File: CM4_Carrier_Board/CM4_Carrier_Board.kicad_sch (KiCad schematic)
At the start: 12 parts, among them J1 Barrel_Jack, J2 DF40C-100DP-0.4V_51_, J3 DF40C-100DP-0.4V_51_, U2 LM2596S-5

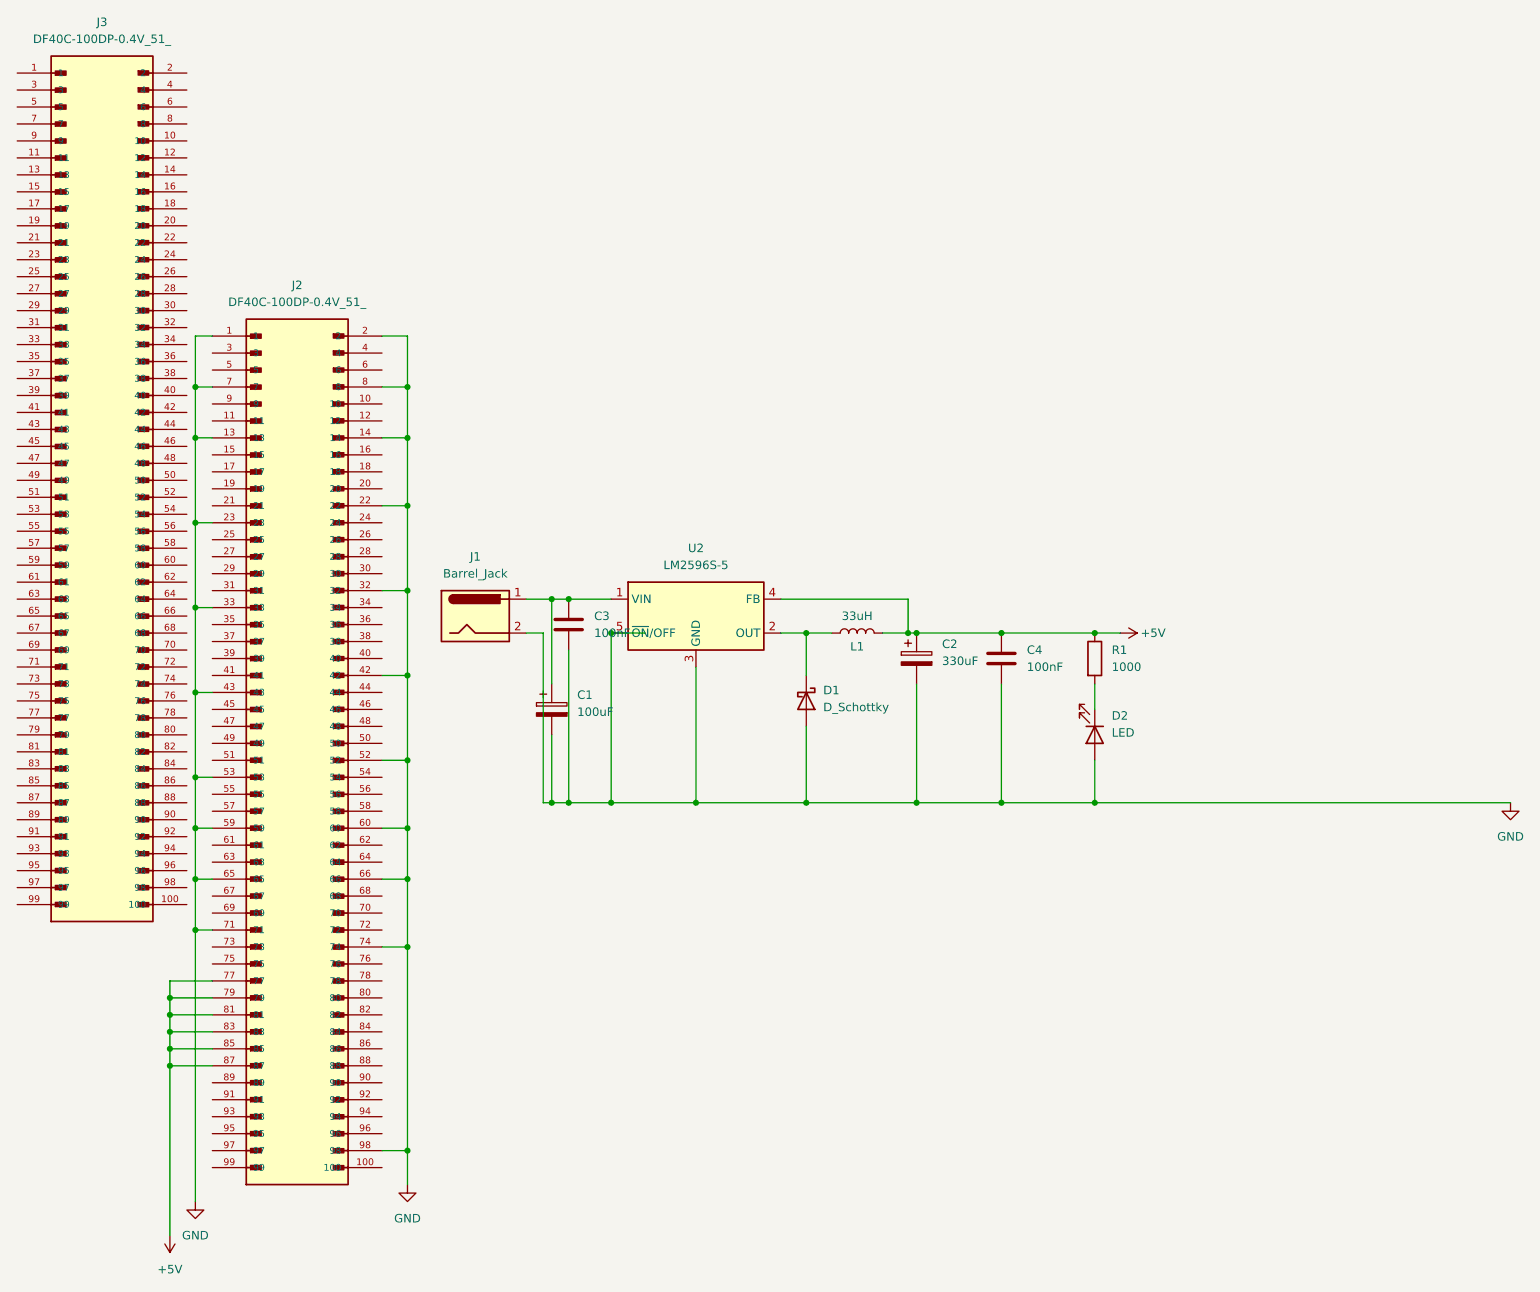
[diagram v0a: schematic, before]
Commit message: Création de la sheet des connecteurs et branchement des signaux de contrôle
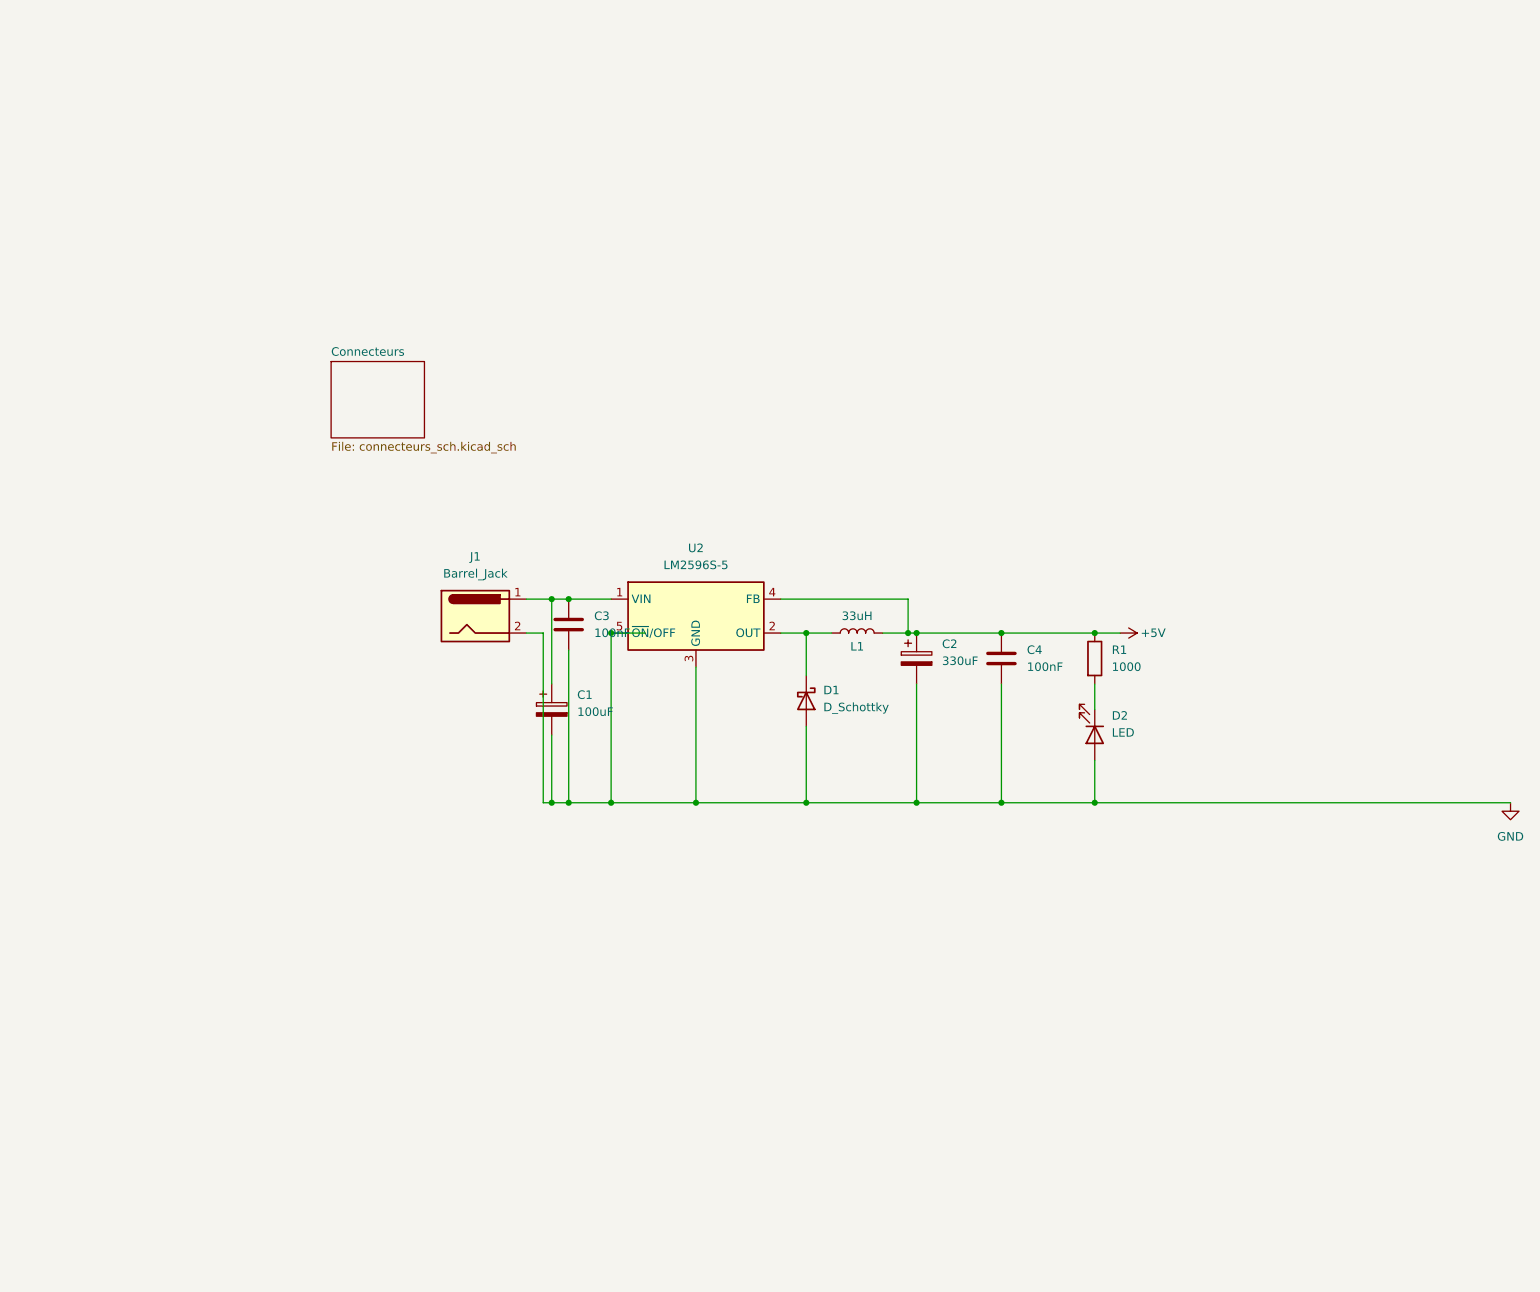
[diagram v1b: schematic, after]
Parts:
- removed J2, J3: DF40C-100DP-0.4V_51_, HIROSE_DF40C-100DP-0.4V_51_, symbol DF40C-100DP-0.4V_51_:DF40C-100DP-0.4V_51_
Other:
- added sheet Connecteurs (connecteurs_sch.kicad_sch)

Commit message: Ajout de la sheet pour le PCIe
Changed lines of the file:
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@@
-	)
-	(junction
-		(at 93.98 99.06)
-		(diameter 0)
-		(color 0 0 0 0)
 	)
 	(junction
@@
 	)
 	(junction
+		(at 123.19 99.06)
+		(diameter 0)
+		(color 0 0 0 0)
+	)
+	(junction
 		(at 152.4 99.06)
 		(diameter 0)
@@
 	)
 	(junction
-		(at 123.19 99.06)
-		(diameter 0)
-		(color 0 0 0 0)
-	)
-	(junction
 		(at 123.19 124.46)
 		(diameter 0)
@@
 	)
 	(junction
+		(at 204.47 124.46)
+		(diameter 0)
+		(color 0 0 0 0)
+	)
+	(junction
 		(at 139.7 124.46)
 		(diameter 0)
@@
 		(color 0 0 0 0)
 	)
-	(wire
-		(pts
-			(xy 166.37 124.46) (xy 228.6 124.46)
+	(junction
+		(at 91.44 93.98)
+		(diameter 0)
+		(color 0 0 0 0)
+	)
+	(wire
+		(pts
+			(xy 166.37 124.46) (xy 204.47 124.46)
 		)
 		(stroke
@@
 	(wire
 		(pts
-			(xy 93.98 99.06) (xy 99.06 99.06)
+			(xy 204.47 124.46) (xy 228.6 124.46)
 		)
 		(stroke
@@
 	(wire
 		(pts
-			(xy 87.63 93.98) (xy 93.98 93.98)
+			(xy 87.63 93.98) (xy 91.44 93.98)
 		)
 		(stroke
@@
 	(wire
 		(pts
+			(xy 93.98 93.98) (xy 91.44 93.98)
+		)
+		(stroke
+			(width 0)
+			(type default)
+		)
+	)
+	(wire
+		(pts
 			(xy 83.82 99.06) (xy 83.82 124.46)
 		)
@@
 	(wire
 		(pts
+			(xy 87.63 124.46) (xy 93.98 124.46)
+		)
+		(stroke
+			(width 0)
+			(type default)
+		)
+	)
+	(wire
+		(pts
 			(xy 119.38 99.06) (xy 123.19 99.06)
 		)
@@
 	(wire
 		(pts
-			(xy 87.63 124.46) (xy 93.98 124.46)
+			(xy 106.68 124.46) (xy 123.19 124.46)
 		)
 		(stroke
@@
 		(pts
 			(xy 87.63 101.6) (xy 87.63 124.46)
-		)
-		(stroke
-			(width 0)
-			(type default)
-		)
-	)
-	(wire
-		(pts
-			(xy 106.68 124.46) (xy 123.19 124.46)
 		)
 		(stroke
@@
 		(in_pos_files yes)
 		(dnp no)
-		(fields_autoplaced yes)
 		(property "Reference" "C3"
-			(at 91.44 96.5199 0)
+			(at 90.424 96.774 0)
 			(show_name no)
 			(do_not_autoplace no)
@@
 		)
 		(property "Value" "100nF"
-			(at 91.44 99.0599 0)
+			(at 87.884 100.838 0)
 			(show_name no)
 			(do_not_autoplace no)
@@
 	)
 	(symbol
+		(lib_id "power:PWR_FLAG")
+		(at 91.44 93.98 0)
+		(unit 1)
+		(body_style 1)
+		(exclude_from_sim no)
+		(in_bom yes)
+		(on_board yes)
+		(in_pos_files yes)
+		(dnp no)
+		(fields_autoplaced yes)
+		(property "Reference" "#FLG01"
+			(at 91.44 92.075 0)
+			(hide yes)
+			(show_name no)
+			(do_not_autoplace no)
+			(effects
+				(font
+					(size 1.27 1.27)
+				)
+			)
+		)
+		(property "Value" "PWR_FLAG"
+			(at 91.44 88.9 0)
+			(show_name no)
+			(do_not_autoplace no)
+			(effects
+				(font
+					(size 1.27 1.27)
+				)
+			)
+		)
+		(property "Footprint" ""
+			(at 91.44 93.98 0)
+			(hide yes)
+			(show_name no)
+			(do_not_autoplace no)
+			(effects
+				(font
+					(size 1.27 1.27)
+				)
+			)
+		)
+		(property "Datasheet" ""
+			(at 91.44 93.98 0)
+			(hide yes)
+			(show_name no)
+			(do_not_autoplace no)
+			(effects
+				(font
+					(size 1.27 1.27)
+				)
+			)
+		)
+		(property "Description" "Special symbol for telling ERC where power comes from"
+			(at 91.44 93.98 0)
+			(hide yes)
+			(show_name no)
+			(do_not_autoplace no)
+			(effects
+				(font
+					(size 1.27 1.27)
+				)
+			)
+		)
+		(pin "1"
+		)
+		(instances
+			(project "CM4_Carrier_Board"
+				(path "/f7b1e63c-7624-492a-bdf8-5574ba799d92"
+					(reference "#FLG01")
+					(unit 1)
+				)
+			)
+		)
+	)
+	(symbol
 		(lib_id "Device:D_Schottky")
 		(at 123.19 109.22 270)
@@
 					(unit 1)
 				)
+			)
+		)
+	)
+	(symbol
+		(lib_id "power:PWR_FLAG")
+		(at 204.47 124.46 0)
+		(unit 1)
+		(body_style 1)
+		(exclude_from_sim no)
+		(in_bom yes)
+		(on_board yes)
+		(in_pos_files yes)
+		(dnp no)
+		(fields_autoplaced yes)
+		(property "Reference" "#FLG02"
+			(at 204.47 122.555 0)
+			(hide yes)
+			(show_name no)
+			(do_not_autoplace no)
+			(effects
+				(font
+					(size 1.27 1.27)
+				)
+			)
+		)
+		(property "Value" "PWR_FLAG"
+			(at 204.47 119.38 0)
+			(show_name no)
+			(do_not_autoplace no)
+			(effects
+				(font
+					(size 1.27 1.27)
+				)
+			)
+		)
+		(property "Footprint" ""
+			(at 204.47 124.46 0)
+			(hide yes)
+			(show_name no)
+			(do_not_autoplace no)
+			(effects
+				(font
+					(size 1.27 1.27)
+				)
+			)
+		)
+		(property "Datasheet" ""
+			(at 204.47 124.46 0)
+			(hide yes)
+			(show_name no)
+			(do_not_autoplace no)
+			(effects
+				(font
+					(size 1.27 1.27)
+				)
+			)
+		)
+		(property "Description" "Special symbol for telling ERC where power comes from"
+			(at 204.47 124.46 0)
+			(hide yes)
+			(show_name no)
+			(do_not_autoplace no)
+			(effects
+				(font
+					(size 1.27 1.27)
+				)
+			)
+		)
+		(pin "1"
+		)
+		(instances
+			(project "CM4_Carrier_Board"
+				(path "/f7b1e63c-7624-492a-bdf8-5574ba799d92"
+					(reference "#FLG02")
+					(unit 1)
+				)

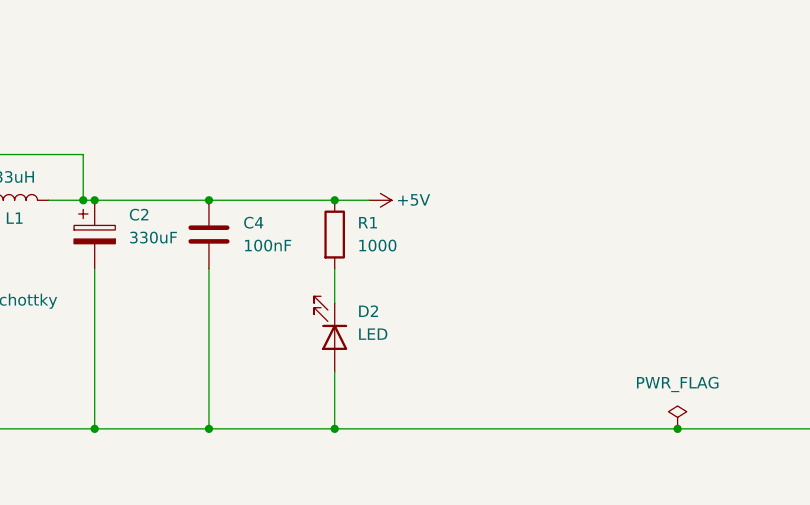
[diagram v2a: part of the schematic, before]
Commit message: Implémentation du cavalier et de la diode d'activation des connecteurs, début d'implémentation du connecteur HDMI
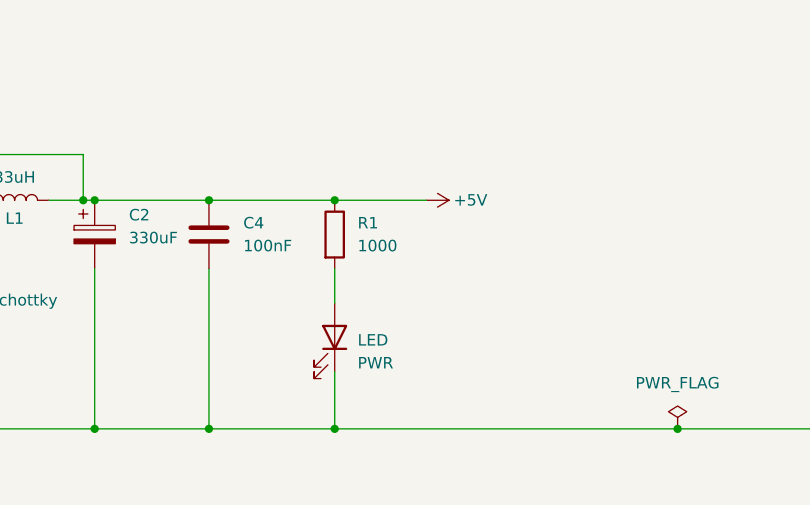
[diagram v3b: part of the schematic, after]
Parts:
- renumbered D2 to PWR
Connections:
- net GND: now also PWR.1 (K); no longer PWR.2 (A)
- net at R1.2: now also PWR.2 (A); no longer PWR.1 (K)
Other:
- moved on the sheet: PWR
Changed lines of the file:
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@@
+	)
+	(junction
+		(at 85.09 124.46)
+		(diameter 0)
+		(color 0 0 0 0)
 	)
 	(junction
@@
 	)
 	(junction
-		(at 85.09 124.46)
-		(diameter 0)
-		(color 0 0 0 0)
-	)
-	(junction
 		(at 166.37 99.06)
 		(diameter 0)
@@
 	(wire
 		(pts
+			(xy 139.7 106.68) (xy 139.7 124.46)
+		)
+		(stroke
+			(width 0)
+			(type default)
+		)
+	)
+	(wire
+		(pts
+			(xy 106.68 104.14) (xy 106.68 124.46)
+		)
+		(stroke
+			(width 0)
+			(type default)
+		)
+	)
+	(wire
+		(pts
+			(xy 166.37 106.68) (xy 166.37 110.49)
+		)
+		(stroke
+			(width 0)
+			(type default)
+		)
+	)
+	(wire
+		(pts
+			(xy 85.09 114.3) (xy 85.09 124.46)
+		)
+		(stroke
+			(width 0)
+			(type default)
+		)
+	)
+	(wire
+		(pts
+			(xy 204.47 124.46) (xy 228.6 124.46)
+		)
+		(stroke
+			(width 0)
+			(type default)
+		)
+	)
+	(wire
+		(pts
+			(xy 85.09 124.46) (xy 87.63 124.46)
+		)
+		(stroke
+			(width 0)
+			(type default)
+		)
+	)
+	(wire
+		(pts
+			(xy 119.38 93.98) (xy 138.43 93.98)
+		)
+		(stroke
+			(width 0)
+			(type default)
+		)
+	)
+	(wire
+		(pts
+			(xy 123.19 99.06) (xy 127 99.06)
+		)
+		(stroke
+			(width 0)
+			(type default)
+		)
+	)
+	(wire
+		(pts
+			(xy 138.43 99.06) (xy 139.7 99.06)
+		)
+		(stroke
+			(width 0)
+			(type default)
+		)
+	)
+	(wire
+		(pts
+			(xy 87.63 93.98) (xy 91.44 93.98)
+		)
+		(stroke
+			(width 0)
+			(type default)
+		)
+	)
+	(wire
+		(pts
+			(xy 139.7 99.06) (xy 152.4 99.06)
+		)
+		(stroke
+			(width 0)
+			(type default)
+		)
+	)
+	(wire
+		(pts
+			(xy 134.62 99.06) (xy 138.43 99.06)
+		)
+		(stroke
+			(width 0)
+			(type default)
+		)
+	)
+	(wire
+		(pts
+			(xy 93.98 99.06) (xy 93.98 124.46)
+		)
+		(stroke
+			(width 0)
+			(type default)
+		)
+	)
+	(wire
+		(pts
+			(xy 152.4 106.68) (xy 152.4 124.46)
+		)
+		(stroke
+			(width 0)
+			(type default)
+		)
+	)
+	(wire
+		(pts
+			(xy 93.98 124.46) (xy 106.68 124.46)
+		)
+		(stroke
+			(width 0)
+			(type default)
+		)
+	)
+	(wire
+		(pts
+			(xy 138.43 93.98) (xy 138.43 99.06)
+		)
+		(stroke
+			(width 0)
+			(type default)
+		)
+	)
+	(wire
+		(pts
+			(xy 123.19 113.03) (xy 123.19 124.46)
+		)
+		(stroke
+			(width 0)
+			(type default)
+		)
+	)
+	(wire
+		(pts
+			(xy 81.28 93.98) (xy 85.09 93.98)
+		)
+		(stroke
+			(width 0)
+			(type default)
+		)
+	)
+	(wire
+		(pts
 			(xy 166.37 124.46) (xy 204.47 124.46)
 		)
@@
 	(wire
 		(pts
-			(xy 139.7 106.68) (xy 139.7 124.46)
-		)
-		(stroke
-			(width 0)
-			(type default)
-		)
-	)
-	(wire
-		(pts
-			(xy 106.68 104.14) (xy 106.68 124.46)
-		)
-		(stroke
-			(width 0)
-			(type default)
-		)
-	)
-	(wire
-		(pts
-			(xy 85.09 114.3) (xy 85.09 124.46)
-		)
-		(stroke
-			(width 0)
-			(type default)
-		)
-	)
-	(wire
-		(pts
-			(xy 204.47 124.46) (xy 228.6 124.46)
-		)
-		(stroke
-			(width 0)
-			(type default)
-		)
-	)
-	(wire
-		(pts
-			(xy 85.09 124.46) (xy 87.63 124.46)
-		)
-		(stroke
-			(width 0)
-			(type default)
-		)
-	)
-	(wire
-		(pts
-			(xy 119.38 93.98) (xy 138.43 93.98)
-		)
-		(stroke
-			(width 0)
-			(type default)
-		)
-	)
-	(wire
-		(pts
-			(xy 123.19 99.06) (xy 127 99.06)
-		)
-		(stroke
-			(width 0)
-			(type default)
-		)
-	)
-	(wire
-		(pts
-			(xy 138.43 99.06) (xy 139.7 99.06)
-		)
-		(stroke
-			(width 0)
-			(type default)
-		)
-	)
-	(wire
-		(pts
-			(xy 87.63 93.98) (xy 91.44 93.98)
-		)
-		(stroke
-			(width 0)
-			(type default)
-		)
-	)
-	(wire
-		(pts
-			(xy 139.7 99.06) (xy 152.4 99.06)
-		)
-		(stroke
-			(width 0)
-			(type default)
-		)
-	)
-	(wire
-		(pts
-			(xy 134.62 99.06) (xy 138.43 99.06)
+			(xy 85.09 93.98) (xy 87.63 93.98)
 		)
 		(stroke
@@
 	(wire
 		(pts
-			(xy 166.37 106.68) (xy 166.37 110.49)
-		)
-		(stroke
-			(width 0)
-			(type default)
-		)
-	)
-	(wire
-		(pts
-			(xy 93.98 99.06) (xy 93.98 124.46)
-		)
-		(stroke
-			(width 0)
-			(type default)
-		)
-	)
-	(wire
-		(pts
-			(xy 152.4 106.68) (xy 152.4 124.46)
-		)
-		(stroke
-			(width 0)
-			(type default)
-		)
-	)
-	(wire
-		(pts
-			(xy 93.98 124.46) (xy 106.68 124.46)
-		)
-		(stroke
-			(width 0)
-			(type default)
-		)
-	)
-	(wire
-		(pts
-			(xy 138.43 93.98) (xy 138.43 99.06)
-		)
-		(stroke
-			(width 0)
-			(type default)
-		)
-	)
-	(wire
-		(pts
-			(xy 123.19 113.03) (xy 123.19 124.46)
-		)
-		(stroke
-			(width 0)
-			(type default)
-		)
-	)
-	(wire
-		(pts
-			(xy 81.28 93.98) (xy 85.09 93.98)
-		)
-		(stroke
-			(width 0)
-			(type default)
-		)
-	)
-	(wire
-		(pts
-			(xy 85.09 93.98) (xy 87.63 93.98)
-		)
-		(stroke
-			(width 0)
-			(type default)
-		)
-	)
-	(wire
-		(pts
 			(xy 152.4 124.46) (xy 166.37 124.46)
 		)
@@
 	(wire
 		(pts
-			(xy 166.37 99.06) (xy 170.18 99.06)
+			(xy 166.37 99.06) (xy 176.53 99.06)
 		)
 		(stroke
@@
 	(symbol
 		(lib_id "power:+5V")
-		(at 170.18 99.06 270)
+		(at 176.53 99.06 270)
 		(unit 1)
 		(body_style 1)
@@
 		(dnp no)
 		(property "Reference" "#PWR04"
-			(at 166.37 99.06 0)
+			(at 172.72 99.06 0)
 			(hide yes)
 			(show_name no)
@@
 		)
 		(property "Value" "+5V"
-			(at 173.228 99.06 90)
+			(at 179.578 99.06 90)
 			(show_name no)
 			(do_not_autoplace no)
@@
 		)
 		(property "Footprint" ""
-			(at 170.18 99.06 0)
+			(at 176.53 99.06 0)
 			(hide yes)
 			(show_name no)
@@
 		)
 		(property "Datasheet" ""
-			(at 170.18 99.06 0)
+			(at 176.53 99.06 0)
 			(hide yes)
 			(show_name no)
@@
 		)
 		(property "Description" "Power symbol creates a global label with name \"+5V\""
-			(at 170.18 99.06 0)
+			(at 176.53 99.06 0)
 			(hide yes)
 			(show_name no)
@@
 		(lib_id "Device:LED")
 		(at 166.37 114.3 270)
+		(mirror x)
 		(unit 1)
 		(body_style 1)
@@
 		(in_pos_files yes)
 		(dnp no)
-		(fields_autoplaced yes)
-		(property "Reference" "D2"
-			(at 168.91 111.4424 90)
+		(property "Reference" "PWR"
+			(at 168.91 117.1576 90)
 			(show_name no)
 			(do_not_autoplace no)
@@
 		)
 		(property "Value" "LED"
-			(at 168.91 113.9824 90)
+			(at 168.91 114.6176 90)
 			(show_name no)
 			(do_not_autoplace no)
@@
 			(project "CM4_Carrier_Board"
 				(path "/f7b1e63c-7624-492a-bdf8-5574ba799d92"
-					(reference "D2")
+					(reference "PWR")
 					(unit 1)
 				)
